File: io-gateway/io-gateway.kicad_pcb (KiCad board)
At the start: 4 copper layers, 155 x 81.5 mm, 52 parts, among them IC1 MAX17673AATI+, J1 1752201, J2 1752201, J3 1752201, J4 Screw_Terminal_01x09, J5 Screw_Terminal_01x09, J6 Screw_Terminal_01x09

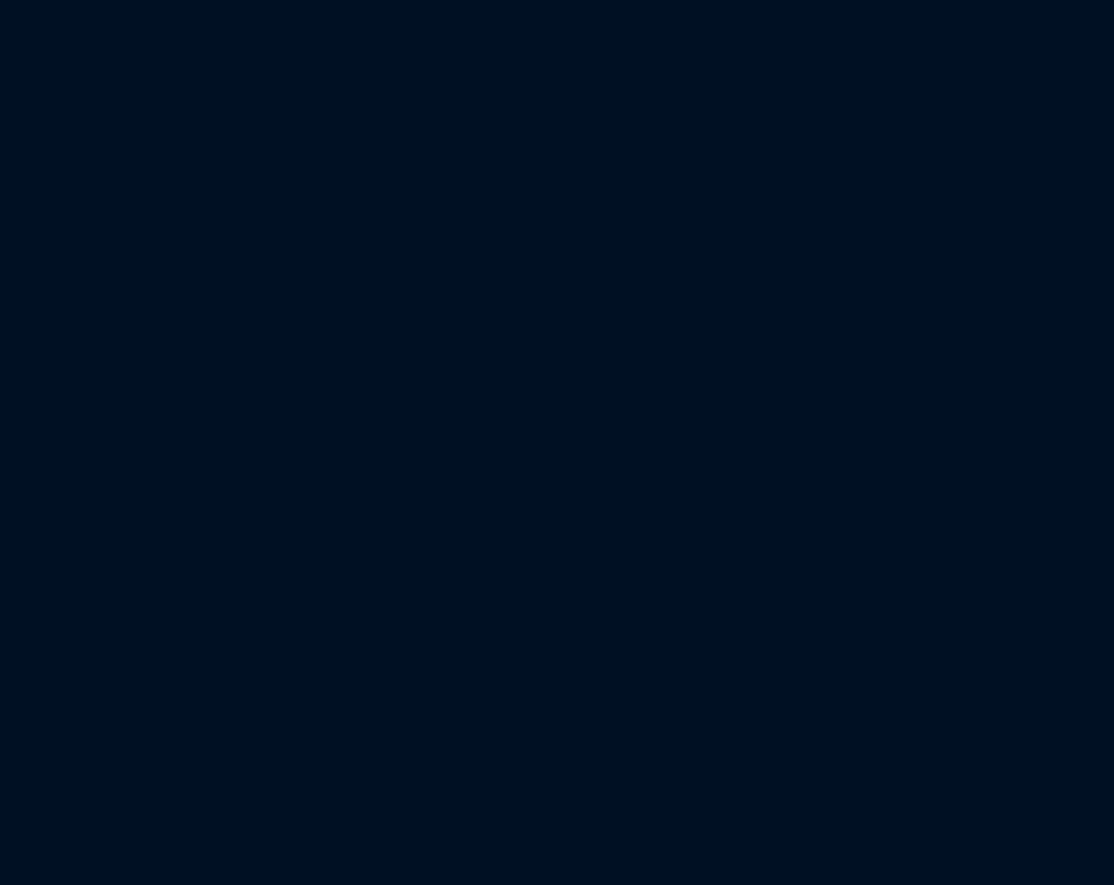
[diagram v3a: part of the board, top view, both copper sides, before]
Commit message: Label Terminal Block Pins
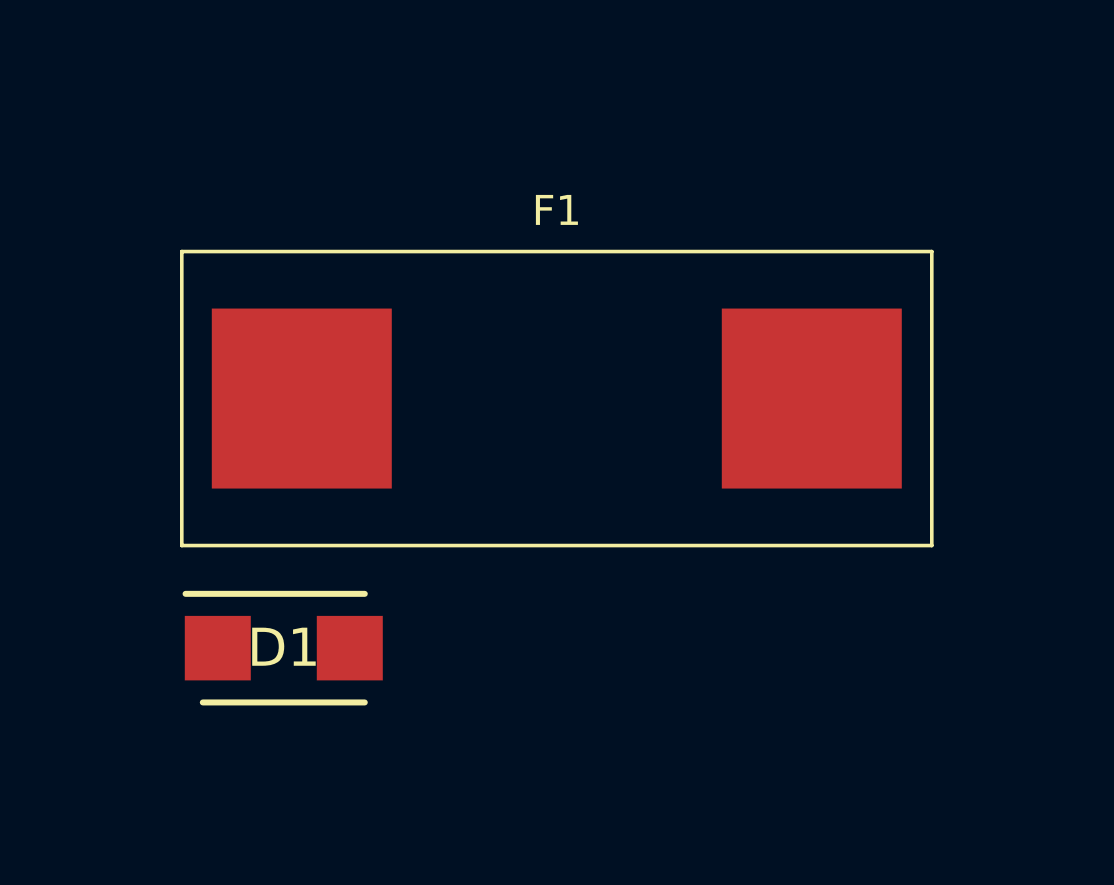
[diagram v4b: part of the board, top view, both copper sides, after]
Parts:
- added D1: SMBJ28A, TVS_Diodes:DIOM5436X244N, F.Cu at (120.3, 84.5)
- added F1: Fuse, Fuse:Fuseholder_Cylinder-5x20mm_Wuerth_696103101002-SMD_Horizontal_Open, F.Cu at (129.4, 76.2)
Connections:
- J1 pad 1: unconnected-(J1-Pad1) -> /Terminal Blocks/VDC_CTRL
- J1 pad 10: unconnected-(J1-Pad10) -> /Terminal Blocks/DIMMER_OUT_1.2
- J1 pad 11: unconnected-(J1-Pad11) -> /Terminal Blocks/DIMMER_OUT_1.3
- J1 pad 12: unconnected-(J1-Pad12) -> /Terminal Blocks/DIMMER_OUT_1.4
- J1 pad 2: unconnected-(J1-Pad2) -> GND
- J1 pad 3: unconnected-(J1-Pad3) -> /Terminal Blocks/RS485_A
- J1 pad 4: unconnected-(J1-Pad4) -> /Terminal Blocks/RS485_B
- J1 pad 5: unconnected-(J1-Pad5) -> /Terminal Blocks/ANALOG_IN_1
- J1 pad 6: unconnected-(J1-Pad6) -> /Terminal Blocks/ANALOG_IN_2
- J1 pad 7: unconnected-(J1-Pad7) -> /Terminal Blocks/VDC_IN1
- J1 pad 8: unconnected-(J1-Pad8) -> /Terminal Blocks/GND_VDC1
- J1 pad 9: unconnected-(J1-Pad9) -> /Terminal Blocks/DIMMER_OUT_1.1
- J2 pad 1: unconnected-(J2-Pad1) -> /Terminal Blocks/VDC_IN_2
- J2 pad 10: unconnected-(J2-Pad10) -> /Terminal Blocks/DIMMER_OUT_3.2
- J2 pad 11: unconnected-(J2-Pad11) -> /Terminal Blocks/DIMMER_OUT_3.3
- J2 pad 12: unconnected-(J2-Pad12) -> /Terminal Blocks/DIMMER_OUT_3.4
- J2 pad 2: unconnected-(J2-Pad2) -> /Terminal Blocks/GND_VDC_2
- J2 pad 3: unconnected-(J2-Pad3) -> /Terminal Blocks/DIMMER_OUT_2.1
- J2 pad 4: unconnected-(J2-Pad4) -> /Terminal Blocks/DIMMER_OUT_2.2
- J2 pad 5: unconnected-(J2-Pad5) -> /Terminal Blocks/DIMMER_OUT_2.3
- J2 pad 6: unconnected-(J2-Pad6) -> /Terminal Blocks/DIMMER_OUT_2.4
- J2 pad 7: unconnected-(J2-Pad7) -> /Terminal Blocks/VDC_IN_3
- J2 pad 8: unconnected-(J2-Pad8) -> /Terminal Blocks/GND_VDC_3
- J2 pad 9: unconnected-(J2-Pad9) -> /Terminal Blocks/DIMMER_OUT_3.1
- J3 pad 1: unconnected-(J3-Pad1) -> /Terminal Blocks/VDC_IN_4
- J3 pad 10: unconnected-(J3-Pad10) -> /Terminal Blocks/DIMMER_OUT_5.2
- J3 pad 11: unconnected-(J3-Pad11) -> /Terminal Blocks/DIMMER_OUT_5.3
- J3 pad 12: unconnected-(J3-Pad12) -> /Terminal Blocks/DIMMER_OUT_5.4
- J3 pad 2: unconnected-(J3-Pad2) -> /Terminal Blocks/GND_VDC_4
- J3 pad 3: unconnected-(J3-Pad3) -> /Terminal Blocks/DIMMER_OUT_4.1
- J3 pad 4: unconnected-(J3-Pad4) -> /Terminal Blocks/DIMMER_OUT_4.2
- J3 pad 5: unconnected-(J3-Pad5) -> /Terminal Blocks/DIMMER_OUT_4.3
- J3 pad 6: unconnected-(J3-Pad6) -> /Terminal Blocks/DIMMER_OUT_4.4
- J3 pad 7: unconnected-(J3-Pad7) -> /Terminal Blocks/VDC_IN_5
- J3 pad 8: unconnected-(J3-Pad8) -> /Terminal Blocks/GND_VDC_5
- J3 pad 9: unconnected-(J3-Pad9) -> /Terminal Blocks/DIMMER_OUT_5.1
- J4 pad 1: unconnected-(J4-Pin_1-Pad1) -> /Terminal Blocks/VAC_IN_1
- J4 pad 2: unconnected-(J4-Pin_2-Pad2) -> /Terminal Blocks/VAC_OUT_1.1
- J4 pad 3: unconnected-(J4-Pin_3-Pad3) -> /Terminal Blocks/VAC_OUT_1.2
- J4 pad 4: unconnected-(J4-Pin_4-Pad4) -> /Terminal Blocks/VAC_IN_2
- J4 pad 5: unconnected-(J4-Pin_5-Pad5) -> /Terminal Blocks/VAC_OUT_2.1
- J4 pad 6: unconnected-(J4-Pin_6-Pad6) -> /Terminal Blocks/VAC_OUT_2.2
- J4 pad 7: unconnected-(J4-Pin_7-Pad7) -> /Terminal Blocks/VAC_IN_3
- J4 pad 8: unconnected-(J4-Pin_8-Pad8) -> /Terminal Blocks/VAC_OUT_3.1
- J4 pad 9: unconnected-(J4-Pin_9-Pad9) -> /Terminal Blocks/VAC_OUT_3.2
- J5 pad 1: unconnected-(J5-Pin_1-Pad1) -> /Terminal Blocks/VAC_IN_7
- J5 pad 2: unconnected-(J5-Pin_2-Pad2) -> /Terminal Blocks/VAC_OUT_7.1
- J5 pad 3: unconnected-(J5-Pin_3-Pad3) -> /Terminal Blocks/VAC_OUT_7.2
- J5 pad 4: unconnected-(J5-Pin_4-Pad4) -> /Terminal Blocks/VAC_IN_8
- J5 pad 5: unconnected-(J5-Pin_5-Pad5) -> /Terminal Blocks/VAC_OUT_8.1
- J5 pad 6: unconnected-(J5-Pin_6-Pad6) -> /Terminal Blocks/VAC_OUT_8.2
- J5 pad 7: unconnected-(J5-Pin_7-Pad7) -> /Terminal Blocks/VAC_IN_9
- J5 pad 8: unconnected-(J5-Pin_8-Pad8) -> /Terminal Blocks/VAC_OUT_9.1
- J5 pad 9: unconnected-(J5-Pin_9-Pad9) -> /Terminal Blocks/VAC_OUT_9.2
- J6 pad 1: unconnected-(J6-Pin_1-Pad1) -> /Terminal Blocks/VAC_IN_4
- J6 pad 2: unconnected-(J6-Pin_2-Pad2) -> /Terminal Blocks/VAC_OUT_4.1
- J6 pad 3: unconnected-(J6-Pin_3-Pad3) -> /Terminal Blocks/VAC_OUT_4.2
- J6 pad 4: unconnected-(J6-Pin_4-Pad4) -> /Terminal Blocks/VAC_IN_5
- J6 pad 5: unconnected-(J6-Pin_5-Pad5) -> /Terminal Blocks/VAC_OUT_5.1
- J6 pad 6: unconnected-(J6-Pin_6-Pad6) -> /Terminal Blocks/VAC_OUT_5.2
- J6 pad 7: unconnected-(J6-Pin_7-Pad7) -> /Terminal Blocks/VAC_IN_6
- J6 pad 8: unconnected-(J6-Pin_8-Pad8) -> /Terminal Blocks/VAC_OUT_6.1
- J6 pad 9: unconnected-(J6-Pin_9-Pad9) -> /Terminal Blocks/VAC_OUT_6.2

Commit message: add relays
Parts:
- added D2: 1N4148, Diode_THT:D_DO-35_SOD27_P7.62mm_Horizontal, F.Cu at (253.3, 52.8)
- added D3: 1N4148, Diode_THT:D_DO-35_SOD27_P7.62mm_Horizontal, F.Cu at (253.3, 56.3)
- added D4: 1N4148, Diode_THT:D_DO-35_SOD27_P7.62mm_Horizontal, F.Cu at (253.3, 59.9)
- added D5: 1N4148, Diode_THT:D_DO-35_SOD27_P7.62mm_Horizontal, F.Cu at (253.3, 63.4)
- added D6: 1N4148, Diode_THT:D_DO-35_SOD27_P7.62mm_Horizontal, F.Cu at (253.3, 67.0)
- added D7: 1N4148, Diode_THT:D_DO-35_SOD27_P7.62mm_Horizontal, F.Cu at (253.3, 70.5)
- added K1: 2071556-2, Relays:20715562, F.Cu at (86.7, 72.8)
- added K2: 2071556-2, Relays:20715562, F.Cu at (57.5, 168.0)
- added K3: 2071556-2, Relays:20715562, F.Cu at (57.0, 181.5)
- added K4: 2071556-2, Relays:20715562, F.Cu at (60.2, 75.7)
- added K5: 2071556-2, Relays:20715562, F.Cu at (221.3, 52.0)
- added K6: 2071556-2, Relays:20715562, F.Cu at (221.3, 65.2)
- added K7: 2071556-2, Relays:20715562, F.Cu at (2.22, 9.95)
- added MCU1: ~, FRDM-MCXN947:FRDM-MCXN947, F.Cu at (144.6, 176.0)
- added Q1: NTR4003NT1G, Package_TO_SOT_SMD:SOT-23-3, F.Cu at (254.3, 25.6)
- added Q2: NTR4003NT1G, Package_TO_SOT_SMD:SOT-23-3, F.Cu at (254.3, 30.3)
- added Q3: NTR4003NT1G, Package_TO_SOT_SMD:SOT-23-3, F.Cu at (254.3, 34.9)
- added Q4: NTR4003NT1G, Package_TO_SOT_SMD:SOT-23-3, F.Cu at (254.3, 39.5)
- added Q5: NTR4003NT1G, Package_TO_SOT_SMD:SOT-23-3, F.Cu at (254.3, 44.1)
- added Q6: NTR4003NT1G, Package_TO_SOT_SMD:SOT-23-3, F.Cu at (254.3, 48.8)
- added R10: 100, Resistor_SMD:R_0603_1608Metric, F.Cu at (253.8, 73.6)
- added R13: 100, Resistor_SMD:R_0603_1608Metric, F.Cu at (253.8, 76.1)
- added R22: 100, Resistor_SMD:R_0603_1608Metric, F.Cu at (253.8, 78.6)
- added R23: 100, Resistor_SMD:R_0603_1608Metric, F.Cu at (253.8, 81.1)
- added R24: 100, Resistor_SMD:R_0603_1608Metric, F.Cu at (253.8, 83.6)
- added R25: 100, Resistor_SMD:R_0603_1608Metric, F.Cu at (253.8, 86.1)
- moved C1 111.8 mm to (-38.3, 72.9)
- moved C15 111.8 mm to (-46.0, 62.7)
- moved C18 111.8 mm to (-56.5, 79.7)
- moved C2 111.8 mm to (-38.3, 75.4)
- moved C3 111.8 mm to (-38.3, 77.9)
- moved C4 111.8 mm to (-38.3, 80.4)
- moved C5 111.8 mm to (-59.9, 64.3)
- moved C6 111.8 mm to (-59.9, 66.8)
- moved C7 111.8 mm to (-59.9, 69.3)
- moved C8 111.8 mm to (-59.9, 71.8)
- moved C9 111.8 mm to (-59.9, 74.3)
- moved D1 111.8 mm to (8.60, 79.7)
- moved F1 111.8 mm to (17.7, 71.4)
- moved IC1 111.8 mm to (-13.7, 83.7)
- moved JP1 111.8 mm to (-48.0, 70.6)
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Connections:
- J4 pad 1: /Terminal Blocks/VAC_IN_1 -> VAC_IN_1
- J4 pad 2: /Terminal Blocks/VAC_OUT_1.1 -> VAC_OUT_1.1
- J4 pad 3: /Terminal Blocks/VAC_OUT_1.2 -> VAC_OUT_1.2
- J4 pad 4: /Terminal Blocks/VAC_IN_2 -> VAC_IN_2
- J4 pad 5: /Terminal Blocks/VAC_OUT_2.1 -> VAC_OUT_2.1
- J4 pad 6: /Terminal Blocks/VAC_OUT_2.2 -> VAC_OUT_2.2
- J4 pad 7: /Terminal Blocks/VAC_IN_3 -> VAC_IN_3
- J4 pad 8: /Terminal Blocks/VAC_OUT_3.1 -> VAC_OUT_3.1
- J4 pad 9: /Terminal Blocks/VAC_OUT_3.2 -> VAC_OUT_3.2

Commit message: Place Relays
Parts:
- removed MCU1: ~, FRDM-MCXN947:FRDM-MCXN947
- added D10: MMSD914, Diode_SMD:D_SOD-123, B.Cu at (113.0, 96.3)
- added D11: MMSD914, Diode_SMD:D_SOD-123, B.Cu at (117.6, 88.0)
- added D12: MMSD914, Diode_SMD:D_SOD-123, B.Cu at (92.8, 96.2)
- added D13: MMSD914, Diode_SMD:D_SOD-123, B.Cu at (105.2, 88.0)
- added D14: MMSD914, Diode_SMD:D_SOD-123, B.Cu at (198.4, 77.6)
- added D15: MMSD914, Diode_SMD:D_SOD-123, B.Cu at (198.4, 98.0)
- added D16: MMSD914, Diode_SMD:D_SOD-123, B.Cu at (186.0, 77.6)
- added D17: MMSD914, Diode_SMD:D_SOD-123, B.Cu at (186.0, 98.0)
- added D18: MMSD914, Diode_SMD:D_SOD-123, B.Cu at (197.8, 106.6)
- added D19: MMSD914, Diode_SMD:D_SOD-123, B.Cu at (142.2, 88.0)
- added D8: MMSD914, Diode_SMD:D_SOD-123, B.Cu at (133.3, 96.3)
- added D9: MMSD914, Diode_SMD:D_SOD-123, B.Cu at (129.8, 88.0)
- added FRDM_MCXN947_1: MCU**, FRDM-MCXN947:FRDM-MCXN947, F.Cu at (165.0, 104.8)
- added K10: 2071556-2, Relays:20715562, F.Cu at (121.4, 87.9)
- added K11: 2071556-2, Relays:20715562, F.Cu at (92.7, 100.2)
- added K12: 2071556-2, Relays:20715562, F.Cu at (109.0, 88.0)
- added K13: 2071556-2, Relays:20715562, F.Cu at (202.2, 77.6)
- added K14: 2071556-2, Relays:20715562, F.Cu at (202.2, 98.0)
- added K15: 2071556-2, Relays:20715562, F.Cu at (189.8, 77.6)
- added K16: 2071556-2, Relays:20715562, F.Cu at (189.8, 98.0)
- added K17: 2071556-2, Relays:20715562, F.Cu at (197.9, 102.8)
- added K18: 2071556-2, Relays:20715562, F.Cu at (146.0, 88.0)
- added K8: 2071556-2, Relays:20715562, F.Cu at (133.7, 88.0)
- added K9: 2071556-2, Relays:20715562, F.Cu at (113.0, 100.2)
- added Q10: NTR4003NT1G, Package_TO_SOT_SMD:SOT-23-3, B.Cu at (114.0, 84.2)
- added Q11: NTR4003NT1G, Package_TO_SOT_SMD:SOT-23-3, B.Cu at (96.6, 92.8)
- added Q12: NTR4003NT1G, Package_TO_SOT_SMD:SOT-23-3, B.Cu at (101.8, 84.2)
- added Q13: NTR4003NT1G, Package_TO_SOT_SMD:SOT-23-3, B.Cu at (194.8, 73.8)
- added Q14: NTR4003NT1G, Package_TO_SOT_SMD:SOT-23-3, B.Cu at (194.8, 94.2)
- added Q15: NTR4003NT1G, Package_TO_SOT_SMD:SOT-23-3, B.Cu at (182.2, 73.9)
- added Q16: NTR4003NT1G, Package_TO_SOT_SMD:SOT-23-3, B.Cu at (182.2, 94.2)
- added Q17: NTR4003NT1G, Package_TO_SOT_SMD:SOT-23-3, B.Cu at (193.9, 110.2)
- added Q18: NTR4003NT1G, Package_TO_SOT_SMD:SOT-23-3, B.Cu at (138.5, 84.2)
- added Q7: NTR4003NT1G, Package_TO_SOT_SMD:SOT-23-3, B.Cu at (137.2, 92.8)
- added Q8: NTR4003NT1G, Package_TO_SOT_SMD:SOT-23-3, B.Cu at (126.2, 84.2)
- added Q9: NTR4003NT1G, Package_TO_SOT_SMD:SOT-23-3, B.Cu at (116.8, 92.5)
- added R26: 100, Resistor_SMD:R_0603_1608Metric, B.Cu at (141.5, 92.0)
- added R27: 100, Resistor_SMD:R_0603_1608Metric, B.Cu at (125.5, 80.0)
- added R28: 100, Resistor_SMD:R_0603_1608Metric, B.Cu at (121.0, 91.8)
- added R29: 100, Resistor_SMD:R_0603_1608Metric, B.Cu at (113.2, 80.0)
- added R30: 100, Resistor_SMD:R_0603_1608Metric, B.Cu at (101.8, 92.8)
- added R31: 100, Resistor_SMD:R_0603_1608Metric, B.Cu at (100.8, 80.0)
- added R32: 100, Resistor_SMD:R_0603_1608Metric, B.Cu at (193.8, 69.5)
- added R33: 100, Resistor_SMD:R_0603_1608Metric, B.Cu at (193.8, 90.0)
- added R34: 100, Resistor_SMD:R_0603_1608Metric, B.Cu at (181.2, 69.5)
- added R35: 100, Resistor_SMD:R_0603_1608Metric, B.Cu at (181.2, 90.0)
- added R36: 100, Resistor_SMD:R_0603_1608Metric, B.Cu at (189.5, 111.0)
- added R37: 100, Resistor_SMD:R_0603_1608Metric, B.Cu at (137.5, 80.0)
- D2, D3, D4, D5, D6, D7: value 1N4148 -> MMSD914; footprint Diode_THT:D_DO-35_SOD27_P7.62mm_Horizontal -> Diode_SMD:D_SOD-123; moved to B.Cu
- IC1, Q1, Q2, Q3, Q4, Q5, Q6, R10, R13, R22, R23, R24, R25: moved to B.Cu
- moved Q4 205.5 mm to (55.8, 92.5), turned to 180 degrees
- moved Q6 205.3 mm to (52.1, 84.3), turned to -90 degrees
- moved D5 204.0 mm to (52.0, 96.3), turned to 90 degrees
- moved R25 202.6 mm to (51.2, 80.0), turned to -90 degrees
- moved D7 198.3 mm to (55.8, 88.0), turned to 180 degrees
- moved Q5 194.0 mm to (64.5, 84.2), turned to -90 degrees
- moved R23 193.8 mm to (60.2, 91.5), turned to 180 degrees
- moved R24 190.3 mm to (63.5, 80.1), turned to -90 degrees
- moved Q2 189.0 mm to (75.9, 92.5), turned to 180 degrees
- moved D6 186.4 mm to (68.2, 88.0), turned to 180 degrees
- moved D3 185.3 mm to (72.3, 96.2), turned to 90 degrees
- moved Q3 184.3 mm to (76.8, 84.2), turned to -90 degrees
- moved R22 178.0 mm to (75.8, 80.0), turned to -90 degrees
- moved Q1 175.4 mm to (89.0, 84.2), turned to -90 degrees
- moved D4 175.2 mm to (80.4, 88.0), turned to 180 degrees
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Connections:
- J5 pad 1: /Terminal Blocks/VAC_IN_7 -> VAC_IN_4
- J5 pad 2: /Terminal Blocks/VAC_OUT_7.1 -> VAC_OUT_4.1
- J5 pad 3: /Terminal Blocks/VAC_OUT_7.2 -> VAC_OUT_4.2
- J5 pad 4: /Terminal Blocks/VAC_IN_8 -> VAC_IN_5
- J5 pad 5: /Terminal Blocks/VAC_OUT_8.1 -> VAC_OUT_5.1
- J5 pad 6: /Terminal Blocks/VAC_OUT_8.2 -> VAC_OUT_5.2
- J5 pad 7: /Terminal Blocks/VAC_IN_9 -> VAC_IN_6
- J5 pad 8: /Terminal Blocks/VAC_OUT_9.1 -> VAC_OUT_6.1
- J5 pad 9: /Terminal Blocks/VAC_OUT_9.2 -> VAC_OUT_6.2
- J6 pad 1: /Terminal Blocks/VAC_IN_4 -> VAC_IN_7
- J6 pad 2: /Terminal Blocks/VAC_OUT_4.1 -> VAC_OUT_7.1
- J6 pad 3: /Terminal Blocks/VAC_OUT_4.2 -> VAC_OUT_7.2
- J6 pad 4: /Terminal Blocks/VAC_IN_5 -> VAC_IN_8
- J6 pad 5: /Terminal Blocks/VAC_OUT_5.1 -> VAC_OUT_8.1
- J6 pad 6: /Terminal Blocks/VAC_OUT_5.2 -> VAC_OUT_8.2
- J6 pad 7: /Terminal Blocks/VAC_IN_6 -> VAC_IN_9
- J6 pad 8: /Terminal Blocks/VAC_OUT_6.1 -> VAC_OUT_9.1
- J6 pad 9: /Terminal Blocks/VAC_OUT_6.2 -> VAC_OUT_9.2
- K3 pad 3: VAC_OUT_3.1 -> VAC_OUT_2.1
- K3 pad 4: VAC_IN_3 -> VAC_IN_2
- K4 pad 3: VAC_OUT_2.1 -> VAC_OUT_2.2
- K5 pad 3: VAC_OUT_2.2 -> VAC_OUT_3.1
- K5 pad 4: VAC_IN_2 -> VAC_IN_3
- K7 pad 1: unconnected-(K7-COIL_1-Pad1) -> +24V
- K7 pad 2: unconnected-(K7-COIL_2-Pad2) -> Net-(D8-A)
- K7 pad 3: unconnected-(K7-COM-Pad3) -> VAC_OUT_4.1
- K7 pad 4: unconnected-(K7-NO-Pad4) -> VAC_IN_4
